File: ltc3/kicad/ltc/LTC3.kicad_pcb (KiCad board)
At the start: 4 copper layers, 202.2 x 150.4 mm, 157 parts, among them IC601 TLP3542, IC701 TLP3542, IC702 TLP3542, IC703 TLP3542, IC704 TLP3542, IC801 TLP3542, IC802 TLP3542, IC803 TLP3542, IC804 TLP3542, J601 RJ45, K601 RELAY_1C, K602 RELAY_1C, P401 43045-1000, P501 BeagleBone_Black_Expansion_He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, P502 BeagleBone_Black_Expansion_He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, P601 BATT-IN, P603 UMBILICAL, P605 43045-0200, P606 S4B-PH-K, P607 43045-0200, P701 43045-1000, P703 43045-0800, P705 43045-0800, P801 43045-1000, P803 43045-0800, P805 43045-0800, Q401 BSS138, Q402 BSS138, Q403 BSS138, Q601 PMV45EN, Q602 PMV45EN, Q603 ZVN4525E6, Q604 ZVN4525E6, Q605 ZVN4525E6, Q701 PMV45EN, Q702 PMV45EN, Q703 PMV45EN, Q704 PMV45EN, Q801 PMV45EN, Q802 PMV45EN, Q803 PMV45EN, Q804 PMV45EN, U401 PTN78020W, U402 LTC2991, U403 PTN78020H, U404 PTN78020H, U501 24C256, U601 CD74HC14, U602 SN65220DBV, U603 741G08

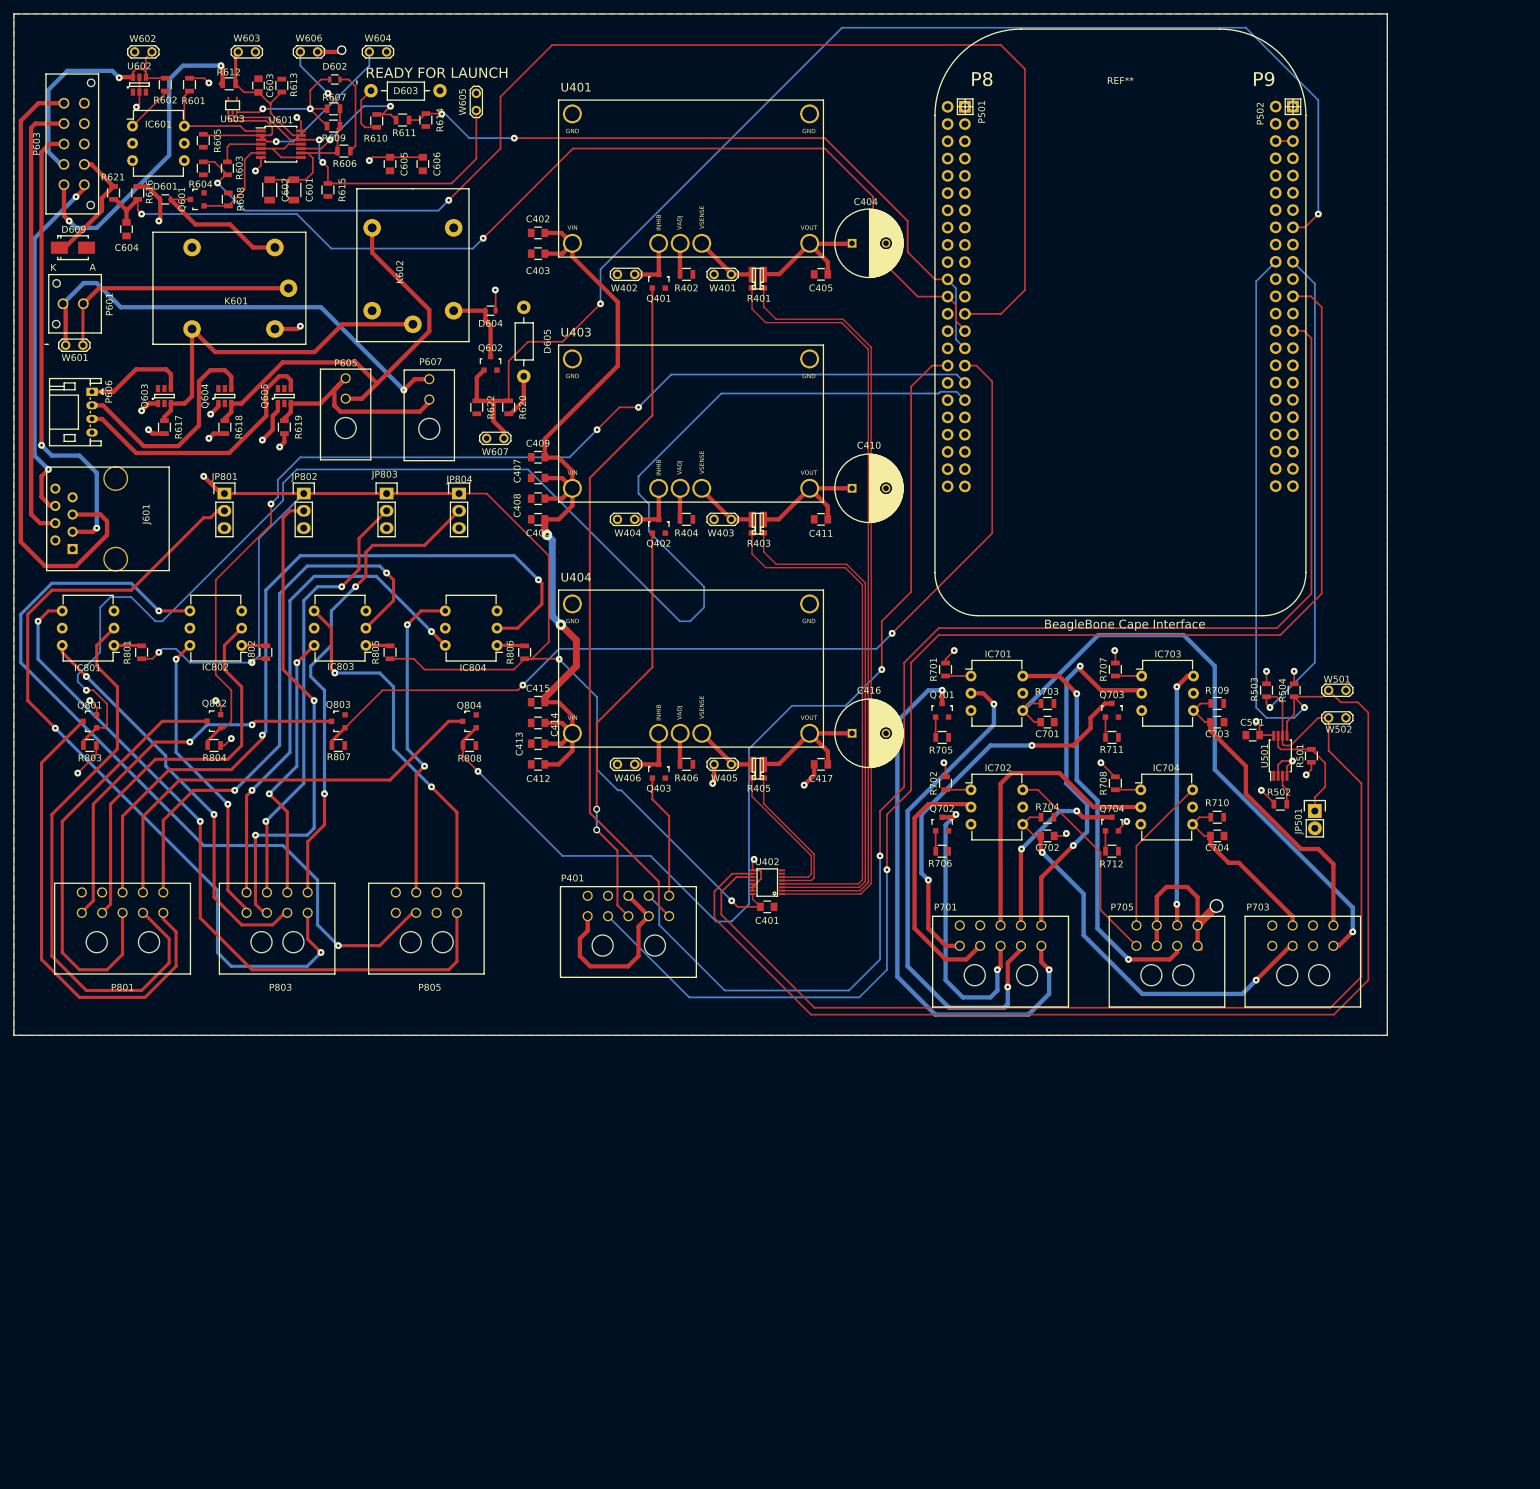
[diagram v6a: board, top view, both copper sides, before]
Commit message: LTC3: LTC BOM and PCB changes.
1. Added RJ45 connector outline to BeagleBone footprint.

2. Rotated BeagleBone footprint on PCB, so that the RJ45 connector
   is on a board edge.

3. Added a notch to the board for BeagleBone RJ45 jack clearance.

4. Updated PCB footprint annotations to align with changes made to the
   LTC schematic in the past few months.

5. Changed BAKERCON MOSFETs to be same part used to activate ignition
   relays.  (Fewer distinct components on the board.)
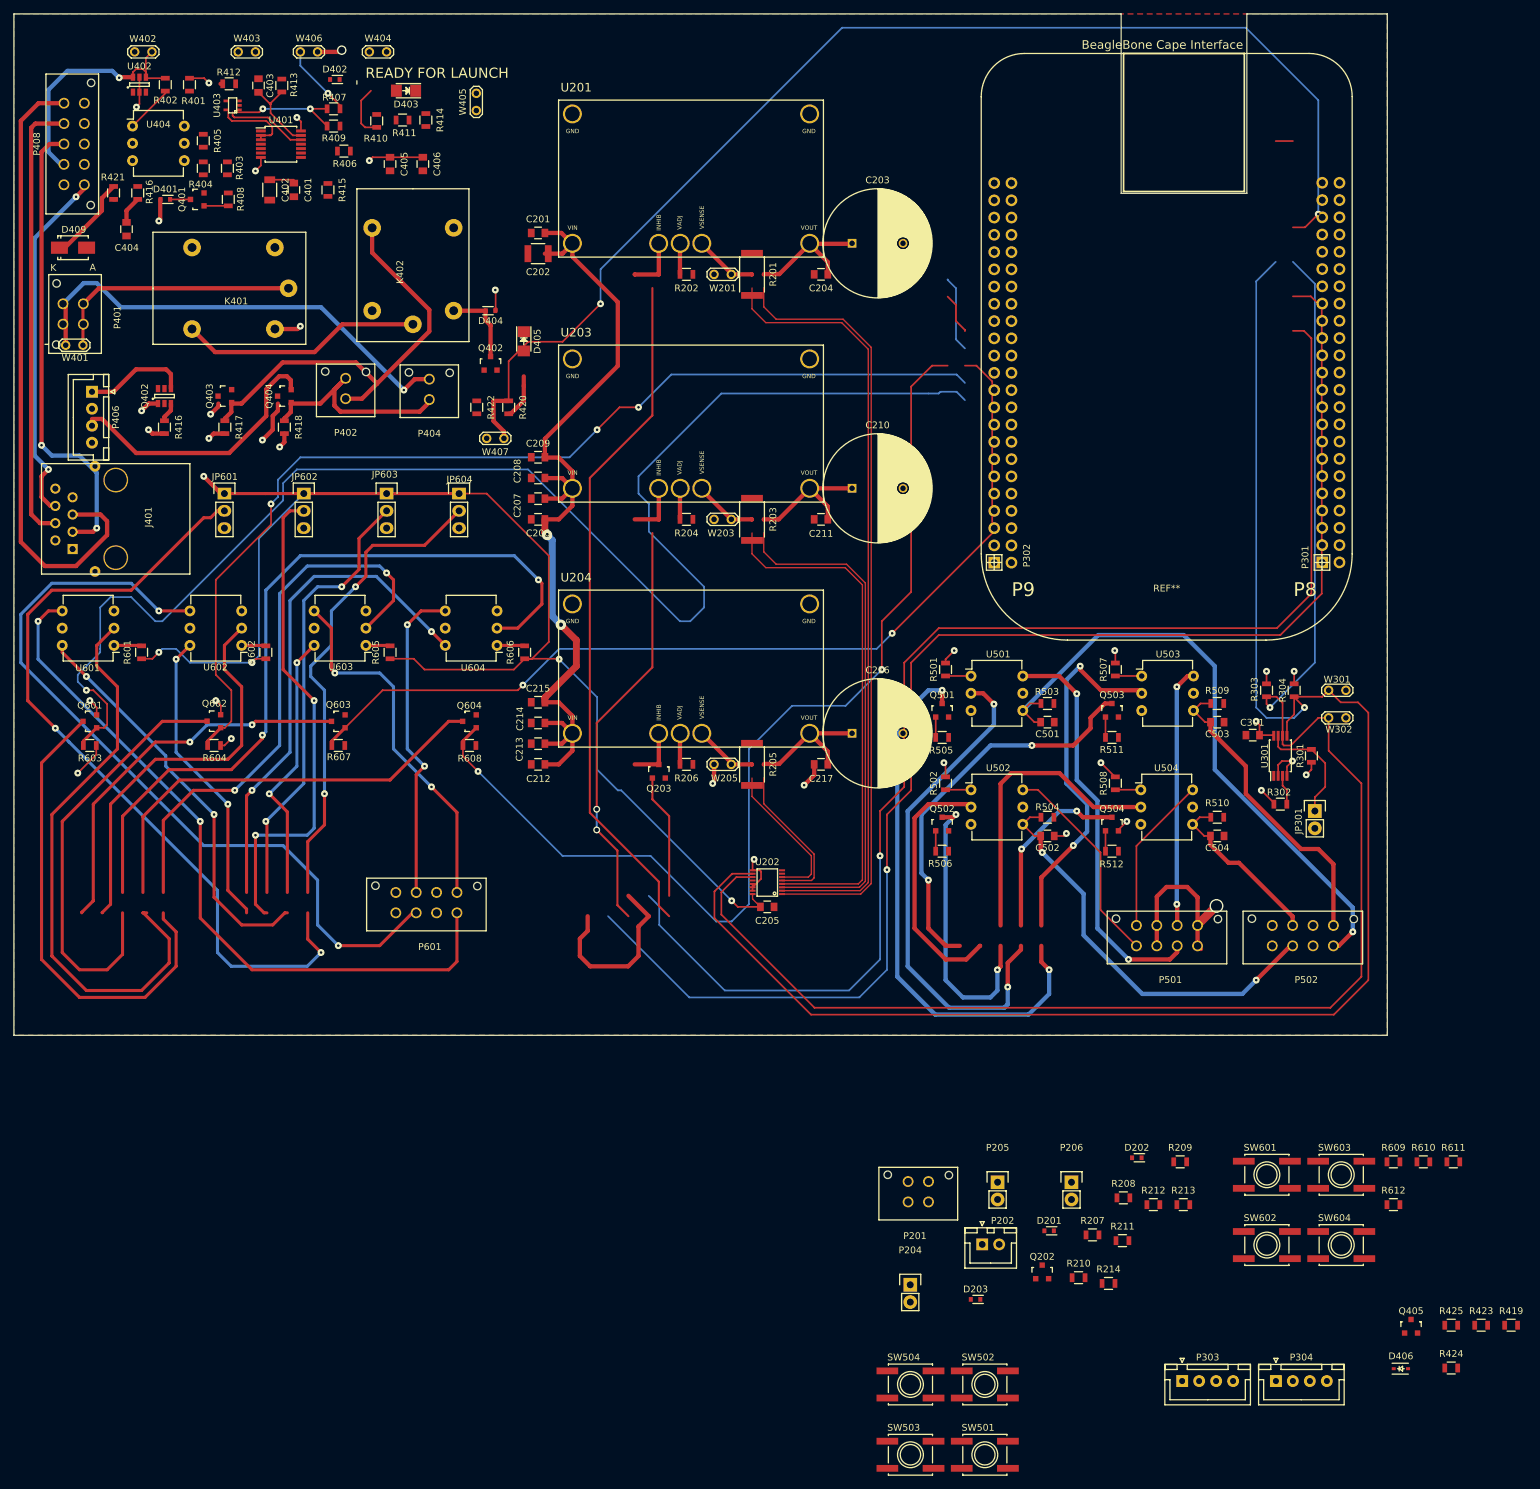
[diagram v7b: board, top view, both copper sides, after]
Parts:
- removed the C403 at (172.2, 82.0)
- removed the C404 at (218.4, 80.5)
- removed C410, C416: 470μ, Capacitors_ThroughHole:C_Radial_D10_L25_P5
- removed C601: 10μ, Capacitors_SMD:C_1206
- removed D601, D602, D604: CDSU4148, Resistors_SMD:R_0603
- removed D603, D605: LED, Choke_Axial_ThroughHole:Choke_Horizontal_RM10mm
- removed J601: RJ45, Connect:RJ45_8
- removed P605, P607: 43045-0200, Connectors_Molex:Molex_Microfit3_Header_02x01_Angled_43045-020x
- removed P606: S4B-PH-K, Connectors_JST:JST_PH_S4B-PH-K_04x2.00mm_Angled
- removed P701, P801: 43045-1000, Connectors_Molex:Molex_Microfit3_Header_02x05_Angled_43045-100x
- removed P703, P705, P803, P805: 43045-0800, Connectors_Molex:Molex_Microfit3_Header_02x04_Angled_43045-080x
- removed the Q401 at (189.9, 86.1)
- removed the Q402 at (189.9, 122.2)
- removed the Q604 at (126.0, 103.0)
- removed Q605: ZVN4525E6, TO_SOT_Packages_SMD:SOT-23-6
- removed the R401 at (203.7, 85.1)
- removed the R403 at (203.7, 121.1)
- removed the R405 at (203.7, 157.2)
- removed the U603 at (127.2, 60.2)
- removed the W402 at (183.8, 85.1)
- removed the W404 at (183.8, 121.1)
- removed the W406 at (183.8, 157.2)
- added C202: 2.2μ, Capacitors_SMD:C_1210, F.Cu at (172.2, 82.0)
- added C203: 470μ, Capacitors_ThroughHole:C_Radial_D16_L25_P7.5, F.Cu at (218.4, 80.5)
- added C210: 470μ, Capacitors_ThroughHole:C_Radial_D16_L25_P7.5, F.Cu at (218.4, 116.6)
- added C216: 470μ, Capacitors_ThroughHole:C_Radial_D16_L25_P7.5, F.Cu at (218.4, 152.6)
- added C401: 10μ, Capacitors_SMD:C_0805, F.Cu at (136.2, 72.6)
- added D201: CDSU4148, Diodes_SMD:SOD-523, F.Cu at (247.4, 225.9)
- added D202: CDSU4148, Diodes_SMD:SOD-523, F.Cu at (260.3, 215.1)
- added D203: CDSU4148, Diodes_SMD:SOD-523, F.Cu at (236.6, 236.0)
- added D401: CDSU4148, Diodes_SMD:SOD-523, F.Cu at (117.3, 74.0)
- added D402: CDSU4148, Diodes_SMD:SOD-523, F.Cu at (142.2, 56.4)
- added D403: RED, LEDs:LED_1206, F.Cu at (152.7, 58.0)
- added D404: CDSU4148, Diodes_SMD:SOD-523, F.Cu at (165.2, 90.4)
- added D405: RED, LEDs:LED_1206, F.Cu at (170.1, 94.9)
- added D406: 3.3V, Diodes_SMD:SOD-323, F.Cu at (299.2, 246.2)
- added J401: RJ45, LTC3:RJ45_8_SHIELDED, F.Cu at (110.0, 121.1)
- added P201: MicroFit header, Connectors_Molex:Molex_Microfit3_Header_02x02_Straight_43045-0428, F.Cu at (229.6, 221.6)
- added P202: XH header, Connectors_JST:JST_XH_B02B-XH-A_02x2.50mm_Straight, F.Cu at (237.5, 227.9)
- added P204: Pin Head 1x2, Pin_Headers:Pin_Header_Straight_1x02, F.Cu at (226.9, 233.8)
- added P205: Pin Head 1x2, Pin_Headers:Pin_Header_Straight_1x02, F.Cu at (239.8, 218.7)
- added P206: Pin Head 1x2, Pin_Headers:Pin_Header_Straight_1x02, F.Cu at (250.7, 218.7)
- added P303: XH header, Connectors_JST:JST_XH_B04B-XH-A_04x2.50mm_Straight, F.Cu at (267.0, 248.0)
- added P304: XH header, Connectors_JST:JST_XH_B04B-XH-A_04x2.50mm_Straight, F.Cu at (280.8, 248.0)
- added P402: MicroFit header, Connectors_Molex:Molex_Microfit3_Header_02x01_Straight_43045-0228, F.Cu at (143.8, 103.4)
- added P404: MicroFit header, Connectors_Molex:Molex_Microfit3_Header_02x01_Straight_43045-0228, F.Cu at (156.1, 103.5)
- added P406: XH header, Connectors_JST:JST_XH_B04B-XH-A_04x2.50mm_Straight, F.Cu at (106.5, 102.4)
- added P501: MicroFit header, Connectors_Molex:Molex_Microfit3_Header_02x04_Straight_43045-0828, F.Cu at (269.2, 183.9)
- added P502: MicroFit header, Connectors_Molex:Molex_Microfit3_Header_02x04_Straight_43045-0828, F.Cu at (289.2, 183.9)
- added Q202: BSS138, TO_SOT_Packages_SMD:SOT-23, F.Cu at (246.4, 231.9)
- added Q403: PMV45EN, TO_SOT_Packages_SMD:SOT-23, F.Cu at (126.0, 103.0)
- added Q404: PMV45EN, TO_SOT_Packages_SMD:SOT-23, F.Cu at (134.8, 103.0)
- added Q405: PMV45EN, TO_SOT_Packages_SMD:SOT-23, F.Cu at (300.7, 239.9)
- added R201: 60m, Resistors_SMD:R_2512, F.Cu at (203.7, 85.1)
- added R203: 60m, Resistors_SMD:R_2512, F.Cu at (203.7, 121.1)
- added R205: 60m, Resistors_SMD:R_2512, F.Cu at (203.7, 157.2)
- added R207: 20k, Resistors_SMD:R_0805, F.Cu at (253.8, 226.5)
- added R208: 20k, Resistors_SMD:R_0805, F.Cu at (258.3, 221.0)
- added R209: 10k, Resistors_SMD:R_0805, F.Cu at (266.7, 215.7)
- added R210: 10k, Resistors_SMD:R_0805, F.Cu at (251.7, 232.8)
- added R211: 36k, Resistors_SMD:R_0805, F.Cu at (258.2, 227.3)
- added R212: 36k, Resistors_SMD:R_0805, F.Cu at (262.7, 222.0)
- added R213: 10k, Resistors_SMD:R_0805, F.Cu at (267.1, 222.0)
- added R214: 10k, Resistors_SMD:R_0805, F.Cu at (256.1, 233.6)
- added R419: 5.1k, Resistors_SMD:R_0805, F.Cu at (315.4, 239.8)
- added R423: 0, Resistors_SMD:R_0805, F.Cu at (311.0, 239.8)
- added R424: 0, Resistors_SMD:R_0805, F.Cu at (306.6, 246.1)
- added R425: 0, Resistors_SMD:R_0805, F.Cu at (306.6, 239.8)
- added R609: 100, Resistors_SMD:R_0805, F.Cu at (298.1, 215.7)
- added R610: 100, Resistors_SMD:R_0805, F.Cu at (302.5, 215.7)
- added R611: 100, Resistors_SMD:R_0805, F.Cu at (306.9, 215.7)
- added R612: 100, Resistors_SMD:R_0805, F.Cu at (298.1, 222.0)
- added SW501: MOMENTARY, Buttons_Switches_SMD:SW_SPST_EVQQ2, F.Cu at (237.9, 258.8)
- added SW502: MOMENTARY, Buttons_Switches_SMD:SW_SPST_EVQQ2, F.Cu at (237.9, 248.5)
- added SW503: MOMENTARY, Buttons_Switches_SMD:SW_SPST_EVQQ2, F.Cu at (227.0, 258.8)
- added SW504: MOMENTARY, Buttons_Switches_SMD:SW_SPST_EVQQ2, F.Cu at (227.0, 248.5)
- added SW601: MOMENTARY, Buttons_Switches_SMD:SW_SPST_EVQQ2, F.Cu at (279.4, 217.6)
- added SW602: MOMENTARY, Buttons_Switches_SMD:SW_SPST_EVQQ2, F.Cu at (279.4, 228.0)
- added SW603: MOMENTARY, Buttons_Switches_SMD:SW_SPST_EVQQ2, F.Cu at (290.4, 217.6)
- added SW604: MOMENTARY, Buttons_Switches_SMD:SW_SPST_EVQQ2, F.Cu at (290.4, 228.0)
- added U403: SN74AHC1G08, TO_SOT_Packages_SMD:SC-70-5, F.Cu at (127.2, 60.2)
- D409: renamed from D609; value 3.3V -> Red, Lg.
- JP301: renamed from JP501; value WR_ENABLE -> Pin Head 1x2
- JP601: renamed from JP801; value Trigger Level -> Pin Head 1x3
- JP602: renamed from JP802; value Trigger Level -> Pin Head 1x3
- JP603: renamed from JP803; value Trigger Level -> Pin Head 1x3
- JP604: renamed from JP804; value Trigger Level -> Pin Head 1x3
- P401: value 43045-1000 -> MicroFit header; footprint Connectors_Molex:Molex_Microfit3_Header_02x05_Angled_43045-100x -> Connectors_Molex:Molex_Microfit3_Header_02x02_Straight_43045-0428
- P408: renamed from P603; value UMBILICAL -> MicroFit header
- P601: value BATT-IN -> MicroFit header; footprint Connectors_Molex:Molex_Microfit3_Header_02x01_Straight_43045-0228 -> Connectors_Molex:Molex_Microfit3_Header_02x04_Straight_43045-0828
- R204: renamed from R404; value 2.91k -> 383k
- R206: renamed from R406; value 2.91k -> 2.87k
- R401: renamed from R601; value 10k -> 62k
- R402: renamed from R602; value 120 -> 10k
- R403: renamed from R603; value 62k -> 100k
- R404: renamed from R604; value 100k -> 120
- R408: renamed from R608; value 10k -> NP
- R409: renamed from R609; value NP -> 10k
- R410: renamed from R610; value 250 -> 5.6k
- R412: renamed from R612; value 5.6k -> 240
- R414: renamed from R614; value 100k -> 10k
- R415: renamed from R615; value 10k -> 100k
- R416: renamed from R616; value 5.1k -> 10k
- R417: renamed from R618; value 30k -> 10k
- R418: renamed from R619; value 30k -> 10k
- R420: renamed from R620; value 250 -> 240
- R421: renamed from R621; value 5.1k -> 10k
- R422: renamed from R622; value 10k -> 5.1k
- U301: renamed from U501; value 24C256 -> CAT24C256
- W401: renamed from W601; value 14.8-16.8V -> TEST
- W402: renamed from W602; value 0/5V -> TEST
- W403: renamed from W603; value 0/5V -> TEST
- W404: renamed from W604; value 0/5V -> TEST
- W405: renamed from W605; value 0/5V -> TEST
- W406: renamed from W606; value 0/5V -> TEST
- W407: renamed from W607; value 0/3.3V -> TEST
- moved P401 124.8 mm to (105.2, 89.4), turned to 90 degrees
- moved P601 105.2 mm to (160.2, 179.1), turned to 0 degrees
- moved REF** 86.8 mm to (288.8, 127.5), turned to 180 degrees
- moved P301 85.2 mm to (287.6, 127.5), turned to 0 degrees
- moved P302 80.3 mm to (239.3, 127.5), turned to 0 degrees
- renumbered C402 to C201, C405 to C204, C401 to C205, C406 to C206, C408 to C207, C407 to C208, C409 to C209, C411 to C211, C412 to C212, C413 to C213, C414 to C214, C415 to C215, C417 to C217, C501 to C301, C602 to C402, C603 to C403, C604 to C404, C605 to C405, C606 to C406, C701 to C501, C702 to C502, C703 to C503, C704 to C504, K601 to K401, K602 to K402, P501 to P301, P502 to P302, Q403 to Q203, Q601 to Q401, Q602 to Q402, Q603 to Q402, Q701 to Q501, Q702 to Q502, Q703 to Q503, Q704 to Q504, Q801 to Q601, Q802 to Q602, Q803 to Q603, Q804 to Q604, R402 to R202, R501 to R301, R502 to R302, R503 to R303, R504 to R304, R605 to R405, R606 to R406, R607 to R407, R611 to R411, R613 to R413, R617 to R416, R701 to R501, R702 to R502, R703 to R503, R704 to R504, R705 to R505, R706 to R506, R707 to R507, R708 to R508, R709 to R509, R710 to R510, R711 to R511, R712 to R512, R801 to R601, R802 to R602, R803 to R603, R804 to R604, R805 to R605, R806 to R606, R807 to R607, R808 to R608, U401 to U201, U402 to U202, U403 to U203, U404 to U204, U601 to U401, U602 to U402, IC601 to U404, IC701 to U501, IC702 to U502, IC703 to U503, IC704 to U504, IC801 to U601, IC802 to U602, IC803 to U603, IC804 to U604, W401 to W201, W403 to W203, W405 to W205, W501 to W301, W502 to W302
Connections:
- net /EXT_TRG_EN_1 renamed /BeagleBone Black Cape/EXT_TRG_EN_1
- net /EXT_TRG_EN_2 renamed /BeagleBone Black Cape/EXT_TRG_EN_2
- net /EXT_TRG_EN_3 renamed /BeagleBone Black Cape/EXT_TRG_EN_3
- net /EXT_TRG_EN_4 renamed /BeagleBone Black Cape/EXT_TRG_EN_4
- net /GPIO_EXT_PWR_1 renamed /External Device Power/EXT_PWR_EN_1
- net /GPIO_EXT_PWR_2 renamed /External Device Power/EXT_PWR_EN_2
- net /GPIO_EXT_PWR_3 renamed /External Device Power/EXT_PWR_EN_3
- net /GPIO_EXT_PWR_4 renamed /External Device Power/EXT_PWR_EN_4
- net /I2C_CLOCK renamed /BeagleBone Black Cape/I2C_CLOCK
- net /I2C_DATA renamed /BeagleBone Black Cape/I2C_DATA
- net Net-(C410-Pad1) renamed /DC-DC Converters/12V_VOUT
- net Net-(C416-Pad1) renamed /DC-DC Converters/19V_VOUT
- net Net-(C701-Pad1) renamed /External Device Power/EXT_PWR_1_OUT
- net Net-(C702-Pad1) renamed /External Device Power/EXT_PWR_2_OUT
- net Net-(C703-Pad1) renamed /External Device Power/EXT_PWR_3_OUT
- net Net-(C704-Pad1) renamed /External Device Power/EXT_PWR_4_OUT
- C204 pad 1: Net-(C404-Pad1) -> /DC-DC Converters/5V_SENSE_H
- C402 pad 1: Net-(C601-Pad1) -> Net-(C401-Pad1)
- C403 pad 1: Net-(C603-Pad1) -> Net-(C403-Pad1)
- C404 pad 1: /UMB_CONn -> /BeagleBone Black Cape/EXT_PWR_EN_4
- D409 pad 1: /Rocket Umbilical & Ignition Control/UMB_CONN_FROM_RKT -> (no net)
- D409 pad 2: GND -> (no net)
- K401 pad 3: Net-(K601-Pad3) -> Net-(K401-Pad3)
- K402 pad 1: Net-(K601-Pad3) -> Net-(K401-Pad3)
- K402 pad 5: Net-(D604-Pad2) -> Net-(D404-Pad2)
- P301 pad 22: /IGN_RTL -> /BeagleBone Black Cape/BQ_EEPROM
- P301 pad 24: /UMB_CONn -> /BeagleBone Black Cape/EXT_PWR_EN_4
- P301 pad 25: /ROCKET_READYn -> /BeagleBone Black Cape/ROCKET_READYn
- P301 pad 27: /UMB_CONn -> /BeagleBone Black Cape/EXT_PWR_EN_4
- P301 pad 29: /IGN_RTL -> /BeagleBone Black Cape/BQ_EEPROM
- P302 pad 23: /12V_ENn -> /BeagleBone Black Cape/12V_ENn
- P302 pad 27: /19V_ENn -> /BeagleBone Black Cape/19V_ENn
- P401 pad 1: /DC-DC Converters/5V_INHIBIT_FET -> /Rocket Umbilical & Ignition Control/IGN_BATT_P
- P401 pad 2: +3V3 -> /Rocket Umbilical & Ignition Control/IGN_BATT_P
- P401 pad 3: /DC-DC Converters/12V_INHIBIT_FET -> GND_IGN
- P401 pad 4: /12V_ENn -> GND_IGN
- P601 pad 1: /Rocket Umbilical & Ignition Control/IGN_BATT_P -> /External Device Triggers/EXT_TRG_1_OUT
- P601 pad 2: GND_IGN -> GND
- Q203 pad 1: /DC-DC Converters/19V_INHIBIT_FET -> /BeagleBone Black Cape/19V_ENn
- Q401 pad 1: Net-(Q601-Pad1) -> Net-(Q401-Pad1)
- Q402 pad 1: /BeagleBone Black Cape/ROCKET_IGNITE -> Net-(K401-Pad3)
- Q402 pad 2: GND -> Net-(Q402-Pad2)
- Q402 pad 3: Net-(D604-Pad2) -> +5V
- Q402 pad 4: Net-(P606-Pad1) -> (no net)
- Q501 pad 3: /External Device Power/EXT_POW_1_FET_D -> Net-(Q501-Pad3)
- Q502 pad 3: /External Device Power/EXT_POW_2_FET_D -> Net-(Q502-Pad3)
- Q503 pad 3: /External Device Power/EXT_POW_3_FET_D -> Net-(Q503-Pad3)
- Q504 pad 3: /External Device Power/EXT_POW_4_FET_D -> Net-(Q504-Pad3)
- Q601 pad 3: /External Device Triggers/EXT_TRG_1_FET_D -> Net-(Q601-Pad3)
- Q602 pad 3: /External Device Triggers/EXT_TRG_2_FET_D -> Net-(Q602-Pad3)
- Q603 pad 3: /External Device Triggers/EXT_TRG_3_FET_D -> Net-(Q603-Pad3)
- Q604 pad 3: /External Device Triggers/EXT_TRG_4_FET_D -> Net-(Q604-Pad3)
- R401 pad 1: +5V -> /BeagleBone Black Cape/ROCKET_READYn
- R401 pad 2: Net-(IC601-Pad6) -> Net-(R401-Pad2)
- R402 pad 1: Net-(IC601-Pad1) -> +5V
- R402 pad 2: /Rocket Umbilical & Ignition Control/ROCKET_READY_5V -> Net-(R402-Pad2)
- R403 pad 1: /ROCKET_READYn -> GND
- R403 pad 2: Net-(R603-Pad2) -> /BeagleBone Black Cape/ROCKET_READYn
- R404 pad 1: GND -> Net-(R404-Pad1)
- R404 pad 2: /ROCKET_READYn -> /Rocket Umbilical & Ignition Control/ROCKET_READY_5V
- R405 pad 1: Net-(R605-Pad1) -> Net-(R405-Pad1)
- R406 pad 1: Net-(C601-Pad1) -> Net-(C401-Pad1)
- R407 pad 1: Net-(C601-Pad1) -> Net-(C401-Pad1)
- R407 pad 2: Net-(D602-Pad1) -> Net-(D402-Pad1)
- R408 pad 1: Net-(Q601-Pad1) -> Net-(C401-Pad1)
- R408 pad 2: GND -> Net-(D402-Pad1)
- R409 pad 1: Net-(C601-Pad1) -> Net-(Q401-Pad1)
- R409 pad 2: Net-(D602-Pad1) -> GND
- R410 pad 1: Net-(R610-Pad1) -> Net-(C403-Pad1)
- R410 pad 2: Net-(D603-Pad2) -> +19V
- R411 pad 1: Net-(R610-Pad1) -> Net-(R411-Pad1)
- R411 pad 2: /IGN_RTL -> /BeagleBone Black Cape/BQ_EEPROM
- R412 pad 1: Net-(C603-Pad1) -> Net-(R411-Pad1)
- R412 pad 2: +19V -> Net-(D403-Pad2)
- R413 pad 1: Net-(C603-Pad1) -> Net-(C403-Pad1)
- R414 pad 1: /IGN_RTL -> Net-(R414-Pad1)
- R415 pad 1: Net-(R615-Pad1) -> /BeagleBone Black Cape/BQ_EEPROM
- R416 pad 1: +5V -> Net-(K401-Pad3)
- R416 pad 2: /UMB_CONn -> GND
- R421 pad 1: /UMB_CONn -> /BeagleBone Black Cape/ROCKET_IGNITE
- R421 pad 2: /Rocket Umbilical & Ignition Control/UMB_CONN_FROM_RKT -> GND
- R422 pad 1: /BeagleBone Black Cape/ROCKET_IGNITE -> /BeagleBone Black Cape/EXT_PWR_EN_4
- R422 pad 2: GND -> /Rocket Umbilical & Ignition Control/UMB_CONN_FROM_RKT
- U201 pad 6: Net-(C404-Pad1) -> /DC-DC Converters/5V_SENSE_H
- U202 pad 1: Net-(R401-Pad4) -> /DC-DC Converters/5V_SENSE_H
- U202 pad 2: Net-(R401-Pad3) -> +5V
- U202 pad 3: Net-(R403-Pad4) -> /DC-DC Converters/12V_SENSE_H
- U202 pad 4: Net-(R403-Pad3) -> /DC-DC Converters/12V_SENSE_L
- U202 pad 5: Net-(R405-Pad4) -> /DC-DC Converters/19V_SENSE_H
- U202 pad 6: Net-(R405-Pad3) -> /DC-DC Converters/19V_SENSE_L
- U401 pad 1: Net-(IC601-Pad6) -> Net-(R405-Pad1)
- U401 pad 10: Net-(R610-Pad1) -> Net-(R411-Pad1)
- U401 pad 11: Net-(U601-Pad11) -> Net-(U401-Pad11)
- U401 pad 12: Net-(R615-Pad1) -> Net-(R414-Pad1)
- U401 pad 13: Net-(C603-Pad1) -> Net-(C403-Pad1)
- U401 pad 2: Net-(R605-Pad1) -> Net-(R401-Pad2)
- U401 pad 3: Net-(R605-Pad1) -> Net-(R402-Pad2)
- U401 pad 4: Net-(R603-Pad2) -> Net-(R405-Pad1)
- U401 pad 5: Net-(U601-Pad11) -> Net-(C401-Pad1)
- U401 pad 6: Net-(Q601-Pad1) -> Net-(U401-Pad11)
- U401 pad 8: Net-(U601-Pad11) -> Net-(Q401-Pad1)
- U401 pad 9: Net-(C601-Pad1) -> Net-(U401-Pad11)
- U404 pad 1: Net-(IC601-Pad1) -> Net-(R404-Pad1)
- U404 pad 6: Net-(IC601-Pad6) -> Net-(R402-Pad2)
- U501 pad 2: /External Device Power/EXT_POW_1_LED_CATH -> Net-(Q501-Pad3)
- U502 pad 2: /External Device Power/EXT_POW_2_LED_CATH -> Net-(Q502-Pad3)
- U503 pad 2: /External Device Power/EXT_POW_3_LED_CATH -> Net-(Q503-Pad3)
- U504 pad 2: /External Device Power/EXT_POW_4_LED_CATH -> Net-(Q504-Pad3)
- U601 pad 2: /External Device Triggers/EXT_TRG_1_LED_CATH -> Net-(Q601-Pad3)
- U601 pad 4: Net-(IC801-Pad4) -> /External Device Triggers/EXT_TRG_1_OUT
- U601 pad 6: /External Device Triggers/EXT_TRG_1_OPTO_RELAY -> Net-(R609-Pad2)
- U602 pad 2: /External Device Triggers/EXT_TRG_2_LED_CATH -> Net-(Q602-Pad3)
- U602 pad 4: Net-(IC802-Pad4) -> /External Device Triggers/EXT_TRG_2_OUT
- U602 pad 6: /External Device Triggers/EXT_TRG_2_OPTO_RELAY -> Net-(R610-Pad2)
- U603 pad 2: /External Device Triggers/EXT_TRG_3_LED_CATH -> Net-(Q603-Pad3)
- U603 pad 4: Net-(IC803-Pad4) -> /External Device Triggers/EXT_TRG_3_OUT
- U603 pad 6: /External Device Triggers/EXT_TRG_3_OPTO_RELAY -> Net-(R611-Pad2)
- U604 pad 2: /External Device Triggers/EXT_TRG_4_LED_CATH -> Net-(Q604-Pad3)
- U604 pad 4: Net-(IC804-Pad4) -> /External Device Triggers/EXT_TRG_4_OUT
- U604 pad 6: /External Device Triggers/EXT_TRG_4_OPTO_RELAY -> Net-(R612-Pad2)
- W403 pad 1: Net-(C603-Pad1) -> Net-(C403-Pad1)
- W404 pad 1: Net-(R605-Pad1) -> Net-(R405-Pad1)
- W405 pad 1: Net-(R615-Pad1) -> Net-(R414-Pad1)
- W406 pad 1: Net-(C601-Pad1) -> Net-(C401-Pad1)
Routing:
- net /BeagleBone Black Cape/19V_ENn: track 0.00 -> 211.8 mm, vias 0 -> 1
- net /BeagleBone Black Cape/12V_ENn: track 0.00 -> 206.1 mm, vias 0 -> 1
- net /12V_ENn: track 206.1 -> 0.00 mm, vias 1 -> 0
- net (no net): track 0.00 -> 198.2 mm, vias 0 -> 4
- net /19V_ENn: track 193.4 -> 0.00 mm, vias 1 -> 0
- net /ROCKET_READYn: track 185.7 -> 0.00 mm, vias 2 -> 0
- net Net-(Q604-Pad3): track 0.00 -> 178.2 mm, vias 0 -> 2
- net Net-(Q501-Pad3): track 0.00 -> 156.3 mm, vias 0 -> 4
- net /UMB_CONn: track 155.9 -> 0.00 mm, vias 2 -> 0
- net Net-(Q601-Pad3): track 0.00 -> 155.5 mm
- net Net-(Q603-Pad3): track 0.00 -> 139.6 mm, vias 0 -> 4
- net /DC-DC Converters/5V_SENSE_H: track 0.00 -> 134.4 mm
- net Net-(Q602-Pad3): track 0.00 -> 122.5 mm
- net Net-(IC802-Pad4): track 116.9 -> 0.00 mm, vias 2 -> 0
- net /External Device Triggers/EXT_TRG_2_OUT: track 0.00 -> 116.9 mm, vias 0 -> 2
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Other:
- outline, holes or cut-outs redrawn
